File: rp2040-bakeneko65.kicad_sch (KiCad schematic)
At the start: 33 parts, among them J1 SM04B-SRSS-TB, J2 SWD, SW85 SW_Push, U1 RP2040, U2 W25Q128JVS, U3 XC6206PxxxMR, U4 SRV05, Y1 12MHz

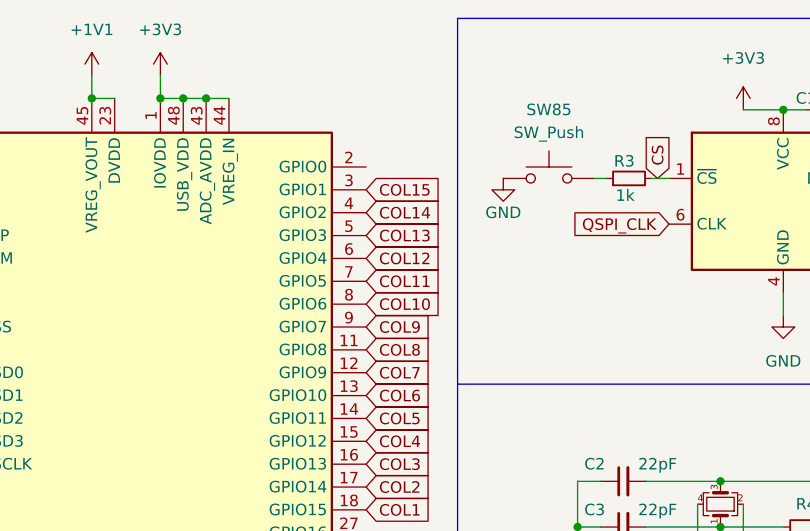
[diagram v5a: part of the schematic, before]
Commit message: more col routing
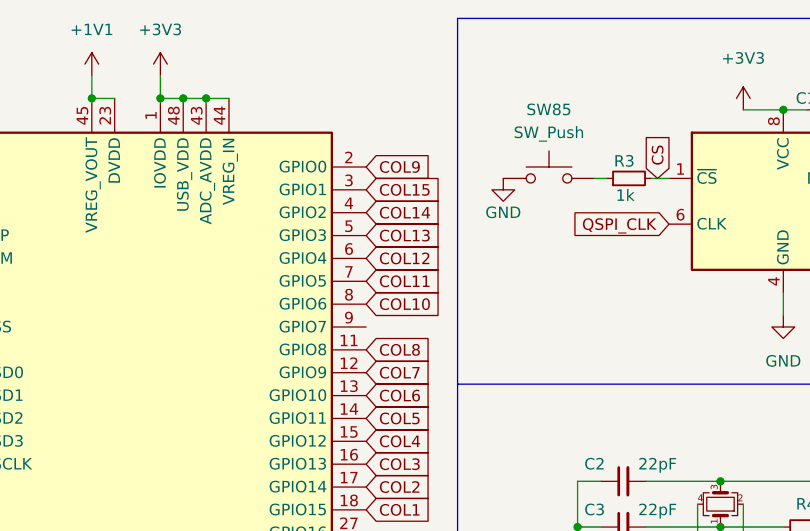
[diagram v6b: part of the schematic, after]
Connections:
- net COL9: now also U1.2 (GPIO0); no longer U1.9 (GPIO7)
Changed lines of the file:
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@@
-    )
-  )
-  (global_label "COL9" (shape input) (at 97.79 46.99 0) (fields_autoplaced)
-    (effects (font (size 1.27 1.27)) (justify left))
-    (property "Intersheetrefs" "${INTERSHEET_REFS}" (at 105.5339 46.99 0)
-      (effects (font (size 1.27 1.27)) (justify left) hide)
     )
   )
@@
     )
   )
+  (global_label "COL9" (shape input) (at 97.79 29.21 0) (fields_autoplaced)
+    (effects (font (size 1.27 1.27)) (justify left))
+    (property "Intersheetrefs" "${INTERSHEET_REFS}" (at 105.5339 29.21 0)
+      (effects (font (size 1.27 1.27)) (justify left) hide)
+    )
+  )

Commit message: Revert "more col routing"
This reverts commit cb50b5119402ddcb1d4d4028dc95a6a712835f21.
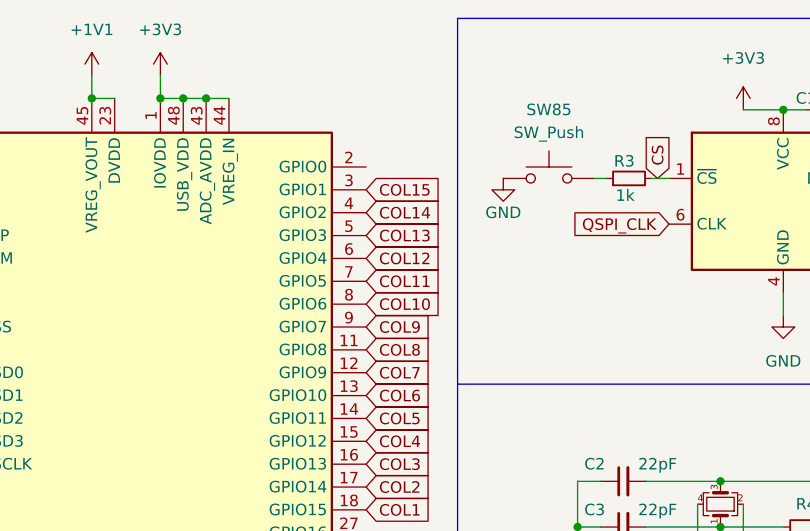
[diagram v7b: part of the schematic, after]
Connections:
- net COL9: now also U1.9 (GPIO7); no longer U1.2 (GPIO0)
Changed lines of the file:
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@@
+    )
+  )
+  (global_label "COL9" (shape input) (at 97.79 46.99 0) (fields_autoplaced)
+    (effects (font (size 1.27 1.27)) (justify left))
+    (property "Intersheetrefs" "${INTERSHEET_REFS}" (at 105.5339 46.99 0)
+      (effects (font (size 1.27 1.27)) (justify left) hide)
     )
   )
@@
     )
   )
-  (global_label "COL9" (shape input) (at 97.79 29.21 0) (fields_autoplaced)
-    (effects (font (size 1.27 1.27)) (justify left))
-    (property "Intersheetrefs" "${INTERSHEET_REFS}" (at 105.5339 29.21 0)
-      (effects (font (size 1.27 1.27)) (justify left) hide)
-    )
-  )

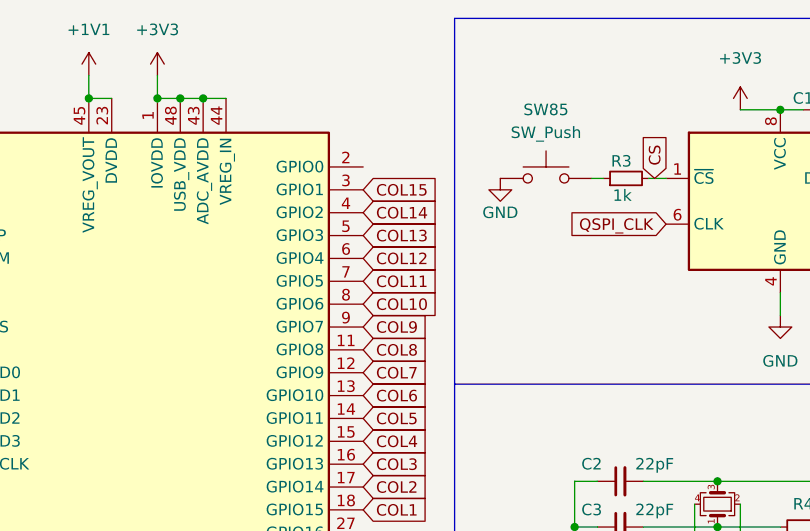
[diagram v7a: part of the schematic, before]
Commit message: MCU reposition + a couple cols
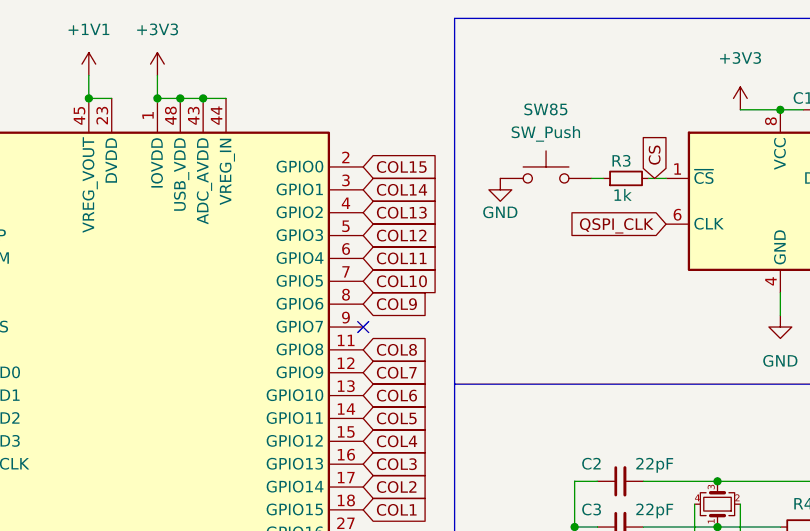
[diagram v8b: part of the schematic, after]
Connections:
- net COL10: now also U1.7 (GPIO5); no longer U1.8 (GPIO6)
- net COL11: now also U1.6 (GPIO4); no longer U1.7 (GPIO5)
- net COL12: now also U1.5 (GPIO3); no longer U1.6 (GPIO4)
- net COL13: now also U1.4 (GPIO2); no longer U1.5 (GPIO3)
- net COL14: now also U1.3 (GPIO1); no longer U1.4 (GPIO2)
- net COL15: now also U1.2 (GPIO0); no longer U1.3 (GPIO1)
- net COL9: now also U1.8 (GPIO6); no longer U1.9 (GPIO7)
- no-connect marks 3 -> 4
